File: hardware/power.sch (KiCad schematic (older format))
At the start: 67 parts, among them P1 CONN_01X02_CBAT, P2 CONN_01X02_FAN, Q1 DMG4712SSS, Q2 DMG4712SSS, U10 MCP1501T-30E, U11 PDM1-S, U12 MIC5225-5.0, U7 MIC5225-5.0, U8 LT3471, U9 R-78E3.3-0.5

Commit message: All DRC/ERC passed
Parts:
- removed W14, W15, W16, W17, W18, W19, W20, W21: TEST_1P, symbol TEST_1P
- added TP10, TP11, TP12, TP13, TP14, TP15, TP16, TP17, TP18, TP9: TEST_POINT, 2kwMotorController:TEST_PAD_1.27mm, symbol TEST_POINT
- C82: renamed from C?; footprint (none) -> Capacitors_SMD:C_0603
- U21: renamed from U?; footprint (none) -> 2kwMotorController:SC-74A
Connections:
- net +12V: now also TP14.1
- net +12V_ISO: now also TP16.1
- net +3V3: now also TP11.1
- net +3V3A: now also TP12.1
- net +5V: now also TP10.1
- net +5V_ISO: now also TP18.1
- net +BATT: now also TP9.1
- net -12V: now also TP13.1
- net PWM_FAN: now also TP15.1
- net FAN_GATE: now reaches Q2.4 (G), R24.1
- net FAN_GATE: now also TP17.1
- net FAN_DRAIN: now reaches D8.2 (A), P2.2 (P2), Q2.5 (D), Q2.6 (D), Q2.7 (D), Q2.8 (D)
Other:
- moved on the sheet: C27, C28, C82, D8, P2, Q2, R24, R25, U21

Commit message: tweaks, testpoints, decluttering
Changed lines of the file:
@@
 FAN_DRAIN
-Wire Wire Line
-	1150 1150 3500 1150
 Wire Wire Line
 	1150 1250 1250 1250
@@
 	10250 4300 10250 4250
 Wire Wire Line
-	7250 1150 7800 1150
-Wire Wire Line
 	7250 1450 7300 1450
 Wire Wire Line
@@
 Connection ~ 6100 1150
 Wire Wire Line
-	7500 1100 7500 1250
-Connection ~ 7500 1150
-Wire Wire Line
 	7500 1550 7500 1650
 Wire Wire Line
@@
 	4150 1050 4150 1250
 Connection ~ 3600 1600
-Wire Wire Line
-	3800 1150 4950 1150
 Wire Wire Line
 	5250 1150 6350 1150
@@
 Connection ~ 5200 5800
 Wire Wire Line
-	3100 1250 3100 1150
+	3100 1150 3100 1250
 Wire Wire Line
 	4150 1600 4150 1550
@@
 Wire Wire Line
 	8350 3050 8350 3100
-Wire Wire Line
-	7800 1150 7800 1100
 Wire Wire Line
 	7900 2600 7900 2700
@@
 Wire Wire Line
 	2600 7250 2600 7300
+Wire Wire Line
+	4150 1150 4950 1150
+Wire Wire Line
+	1150 1150 3100 1150
+Wire Wire Line
+	7500 1250 7500 1100
+Wire Wire Line
+	7250 1150 7500 1150
+Connection ~ 7500 1150
 $EndSCHEMATC

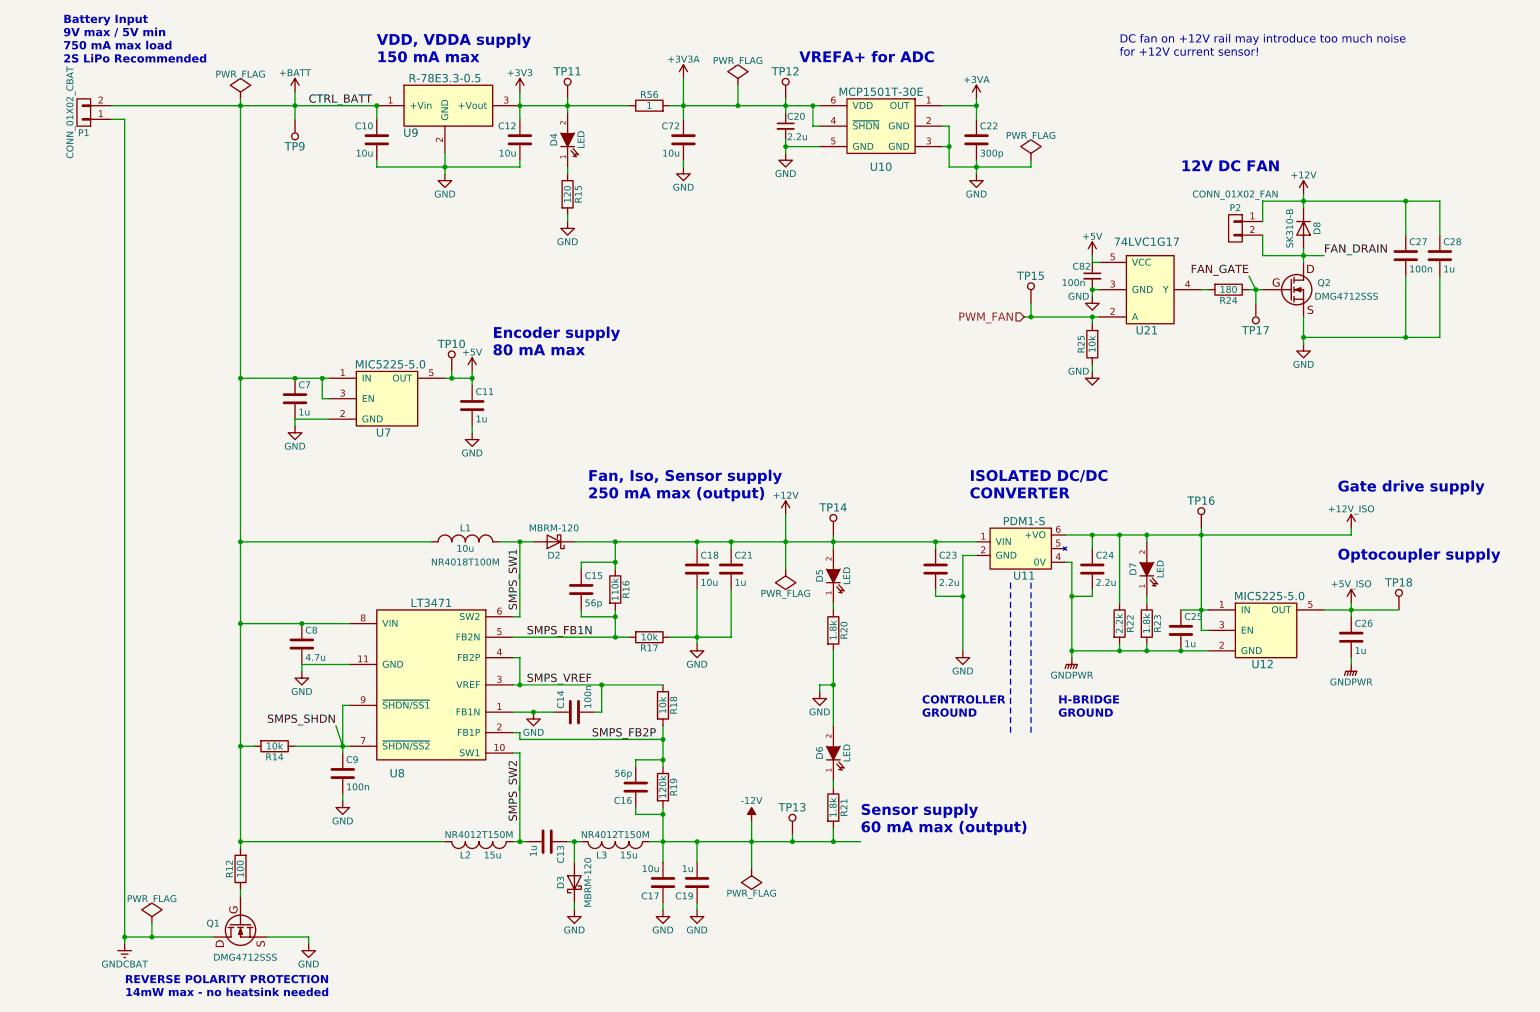
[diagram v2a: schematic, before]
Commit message: Create and verify full Digikey BOM
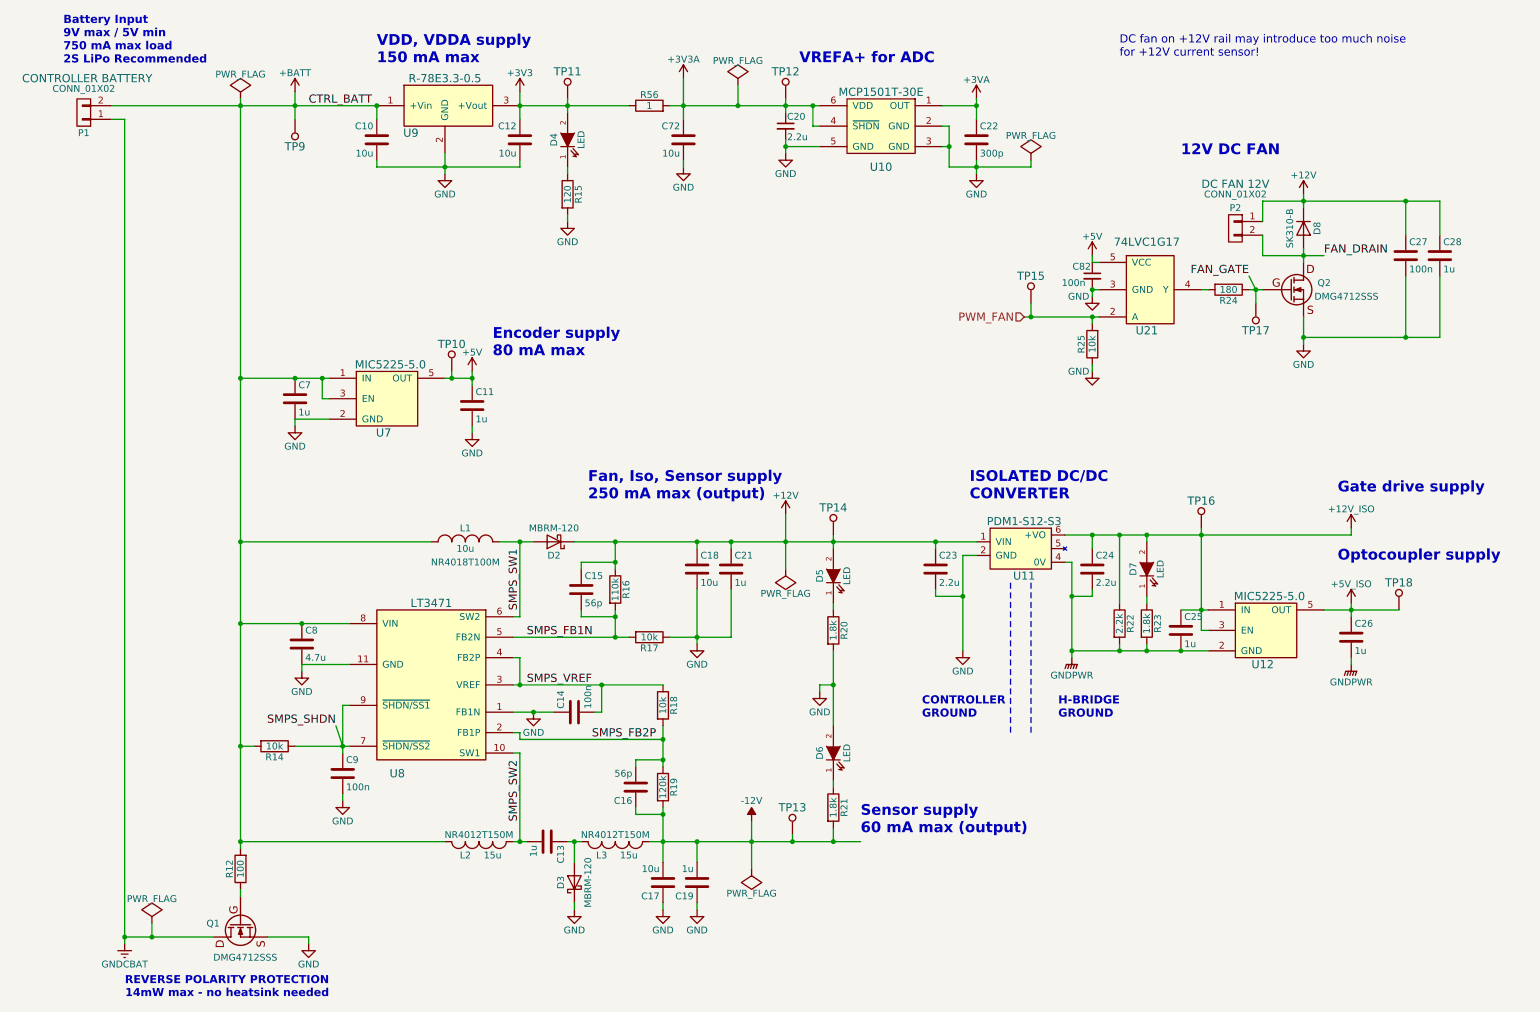
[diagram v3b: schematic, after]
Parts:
- C10: footprint Capacitors_SMD:C_0603 -> Capacitors_SMD:C_0805; Voltage (none) -> 16V
- C11, C12, C20, C22, C7, C72: Voltage (none) -> 16V
- C14, C15, C16, C17, C18, C19, C21, C23, C24, C25, C26, C27, C28, C8, C82, C9: Voltage (none) -> 25V
- P1: value CONN_01X02_CBAT -> CONN_01X02; Use (none) -> CONTROLLER BATTERY
- P2: value CONN_01X02_FAN -> CONN_01X02; Use (none) -> DC FAN 12V
- U11: value PDM1-S -> PDM1-S12-S3
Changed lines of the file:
@@
 P 950 1200
 F 0 "P1" H 950 1350 50  0000 C CNN
-F 1 "CONN_01X02_CBAT" V 1050 1200 50  0000 C CNN
+F 1 "CONN_01X02" H 950 1025 50  0000 C CNN
 F 2 "2kwMotorController:TERM_2P_2-5_1990009" H 950 1200 50  0001 C CNN
 F 3 "" H 950 1200 50  0000 C CNN
+F 4 "CONTROLLER BATTERY" H 925 950 60  0000 C CNN "Use"
 	1    950  1200
 	-1   0    0    1
@@
 P 7800 4400
 F 0 "U11" H 7850 4200 59  0000 C CNN
-F 1 "PDM1-S" H 7850 4600 59  0000 C CNN
+F 1 "PDM1-S12-S3" H 7850 4600 59  0000 C CNN
 F 2 "2kwMotorController:PDM2-S" H 7850 4400 59  0001 C CNN
 F 3 "" H 7850 4400 59  0000 C CNN
@@
 F 2 "Capacitors_SMD:C_0805" H 5488 4400 50  0001 C CNN
 F 3 "" H 5450 4550 50  0000 C CNN
+F 4 "25V" H 5450 4550 60  0001 C CNN "Voltage"
 	1    5450 4550
 	1    0    0    -1
@@
 F 2 "Capacitors_SMD:C_0805" H 5238 6700 50  0001 C CNN
 F 3 "" H 5200 6850 50  0000 C CNN
+F 4 "25V" H 5200 6850 60  0001 C CNN "Voltage"
 	1    5200 6850
 	-1   0    0    1
@@
 F 2 "Capacitors_SMD:C_0603" H 5038 6000 50  0001 C CNN
 F 3 "" H 5000 6150 50  0000 C CNN
+F 4 "25V" H 5000 6150 60  0001 C CNN "Voltage"
 	1    5000 6150
 	-1   0    0    1
@@
 F 2 "Capacitors_SMD:C_0603" H 2888 5900 50  0001 C CNN
 F 3 "" H 2850 6050 50  0000 C CNN
+F 4 "25V" H 2850 6050 60  0001 C CNN "Voltage"
 	1    2850 6050
 	1    0    0    -1
@@
 F 2 "Capacitors_SMD:C_0603" H 4638 4550 50  0001 C CNN
 F 3 "" H 4600 4700 50  0000 C CNN
+F 4 "25V" H 4600 4700 60  0001 C CNN "Voltage"
 	1    4600 4700
 	1    0    0    -1
@@
 F 2 "Capacitors_SMD:C_0603" H 2588 4950 50  0001 C CNN
 F 3 "" H 2550 5100 50  0000 C CNN
+F 4 "25V" H 2550 5100 60  0001 C CNN "Voltage"
 	1    2550 5100
 	1    0    0    -1
@@
 F 2 "Capacitors_SMD:C_0603" H 4588 5450 50  0001 C CNN
 F 3 "" H 4550 5600 50  0000 C CNN
+F 4 "25V" H 4550 5600 60  0001 C CNN "Voltage"
 	1    4550 5600
 	0    -1   -1   0
@@
 F 2 "Capacitors_SMD:C_0603" H 7538 1250 50  0001 C CNN
 F 3 "" H 7500 1400 50  0000 C CNN
+F 4 "16V" H 7500 1400 60  0001 C CNN "Voltage"
 	1    7500 1400
 	1    0    0    -1
@@
 F 0 "C10" H 3125 1500 50  0000 L CNN
 F 1 "10u" H 3125 1300 50  0000 L CNN
-F 2 "Capacitors_SMD:C_0603" H 3138 1250 50  0001 C CNN
+F 2 "Capacitors_SMD:C_0805" H 3138 1250 50  0001 C CNN
 F 3 "" H 3100 1400 50  0000 C CNN
+F 4 "16V" H 3100 1400 60  0001 C CNN "Voltage"
 	1    3100 1400
 	-1   0    0    -1
@@
 F 2 "Capacitors_SMD:C_0805" H 4188 1250 50  0001 C CNN
 F 3 "" H 4150 1400 50  0000 C CNN
+F 4 "16V" H 4150 1400 60  0001 C CNN "Voltage"
 	1    4150 1400
 	-1   0    0    -1
@@
 F 2 "Capacitors_SMD:C_0603" H 10288 4900 50  0001 C CNN
 F 3 "" H 10250 5050 50  0000 C CNN
+F 4 "25V" H 10250 5050 60  0001 C CNN "Voltage"
 	1    10250 5050
 	1    0    0    -1
@@
 F 2 "Capacitors_SMD:C_0603" H 9038 4850 50  0001 C CNN
 F 3 "" H 9000 5000 50  0000 C CNN
+F 4 "25V" H 9000 5000 60  0001 C CNN "Voltage"
 	1    9000 5000
 	1    0    0    -1
@@
 F 2 "Capacitors_SMD:C_0603" H 3838 3200 50  0001 C CNN
 F 3 "" H 3800 3350 50  0000 C CNN
+F 4 "16V" H 3800 3350 60  0001 C CNN "Voltage"
 	1    3800 3350
 	1    0    0    -1
@@
 F 2 "Capacitors_SMD:C_0603" H 2538 3150 50  0001 C CNN
 F 3 "" H 2500 3300 50  0000 C CNN
+F 4 "16V" H 2500 3300 60  0001 C CNN "Voltage"
 	1    2500 3300
 	1    0    0    -1
@@
 P 9400 2050
 F 0 "P2" H 9400 2200 50  0000 C CNN
-F 1 "CONN_01X02_FAN" H 9400 2300 50  0000 C CNN
+F 1 "CONN_01X02" H 9400 2300 50  0000 C CNN
 F 2 "2kwMotorController:TERM_2P_2-5_1990009" H 9400 2050 50  0001 C CNN
-F 3 "" H 9400 2050 50  0000 C CNN
+F 3 "1990009" H 9400 2050 50  0001 C CNN
+F 4 "DC FAN 12V" H 9400 2375 60  0000 C CNN "Use"
 	1    9400 2050
 	-1   0    0    -1
@@
 Text HLabel 7850 2700 0    60   Input ~ 0
 PWM_FAN
-Text Notes 9000 1650 0    79   ~ 16
+Text Notes 9000 1525 0    79   ~ 16
 12V DC FAN
 $Comp
@@
 F 2 "Capacitors_SMD:C_0603" H 10688 2100 50  0001 C CNN
 F 3 "" H 10650 2250 50  0000 C CNN
+F 4 "25V" H 10650 2250 60  0001 C CNN "Voltage"
 	1    10650 2250
 	1    0    0    -1
@@
 F 2 "Capacitors_SMD:C_0603" H 10938 2100 50  0001 C CNN
 F 3 "" H 10900 2250 50  0000 C CNN
+F 4 "25V" H 10900 2250 60  0001 C CNN "Voltage"
 	1    10900 2250
 	1    0    0    -1
@@
 F 2 "Capacitors_SMD:C_0603" H 7238 4400 50  0001 C CNN
 F 3 "" H 7200 4550 50  0000 C CNN
+F 4 "25V" H 7200 4550 60  0001 C CNN "Voltage"
 	1    7200 4550
 	1    0    0    -1
@@
 F 2 "Capacitors_SMD:C_0603" H 8388 4400 50  0001 C CNN
 F 3 "" H 8350 4550 50  0000 C CNN
+F 4 "25V" H 8350 4550 60  0001 C CNN "Voltage"
 	1    8350 4550
 	1    0    0    -1
@@
 F 2 "Capacitors_SMD:C_0603" H 5488 6700 50  0001 C CNN
 F 3 "" H 5450 6850 50  0000 C CNN
+F 4 "25V" H 5450 6850 60  0001 C CNN "Voltage"
 	1    5450 6850
 	-1   0    0    1
@@
 F 2 "Capacitors_SMD:C_0603" H 5738 4400 50  0001 C CNN
 F 3 "" H 5700 4550 50  0000 C CNN
+F 4 "25V" H 5700 4550 60  0001 C CNN "Voltage"
 	1    5700 4550
 	1    0    0    -1
@@
 F 2 "Capacitors_SMD:C_0603" H 6100 1300 50  0001 C CNN
 F 3 "" H 6100 1300 50  0000 C CNN
+F 4 "16V" H 6100 1300 60  0001 C CNN "Voltage"
 	1    6100 1300
 	1    0    0    -1
@@
 F 2 "Capacitors_SMD:C_0805" H 5388 1250 50  0001 C CNN
 F 3 "" H 5350 1400 50  0000 C CNN
+F 4 "16V" H 5350 1400 60  0001 C CNN "Voltage"
 	1    5350 1400
 	-1   0    0    -1
@@
 F 2 "Capacitors_SMD:C_0603" H 8350 2400 50  0001 C CNN
 F 3 "" H 8350 2400 50  0000 C CNN
+F 4 "25V" H 8350 2400 60  0001 C CNN "Voltage"
 	1    8350 2400
 	-1   0    0    -1

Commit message: Open Loop Test Code
Rough version of control task for open loop testing of H-bridge
Rough version of sensor code
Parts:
- D4, D5, D6, D7: symbol LED -> LED-RESCUE-2kwMotorController
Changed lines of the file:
@@
 EESchema Schematic File Version 2
+LIBS:2kwMotorController-rescue
 LIBS:power
 LIBS:device
@@
 $EndComp
 $Comp
-L LED D7
+L LED-RESCUE-2kwMotorController D7
 U 1 1 5985847D
 P 8750 4550
@@
 Gate drive supply
 $Comp
-L LED D4
+L LED-RESCUE-2kwMotorController D4
 U 1 1 59B58EF7
 P 4500 1400
@@
 $EndComp
 $Comp
-L LED D5
+L LED-RESCUE-2kwMotorController D5
 U 1 1 59B74B7C
 P 6450 4600
@@
 $EndComp
 $Comp
-L LED D6
+L LED-RESCUE-2kwMotorController D6
 U 1 1 59B7727F
 P 6450 5900

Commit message: Revised layout mostly complete
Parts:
- removed P2: CONN_01X02, 2kwMotorController:TERM_2P_2-5_1990009, symbol CONN_01X02
- added P2: CONN_01X04, 2kwMotorController:TERM_4P_2-4_1990025, symbol CONN_01X04
- P1: footprint 2kwMotorController:TERM_2P_2-5_1990009 -> Pin_Headers:Pin_Header_Straight_1x02
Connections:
- net +12V: now also P2.1 (P1), P2.3 (P3)
- net FAN_DRAIN: now also P2.2 (P2), P2.4 (P4)

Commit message: Bugfixes and python terminal display
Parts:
- R20, R21: value 1.8k -> 3.9k

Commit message: Update BOM
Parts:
- U11: value PDM1-S12-S3 -> PDM1-S12-S12
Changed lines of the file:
@@
 P 7800 4400
 F 0 "U11" H 7850 4200 59  0000 C CNN
-F 1 "PDM1-S12-S3" H 7850 4600 59  0000 C CNN
+F 1 "PDM1-S12-S12" H 7850 4600 59  0000 C CNN
 F 2 "2kwMotorController:PDM2-S" H 7850 4400 59  0001 C CNN
 F 3 "" H 7850 4400 59  0000 C CNN
